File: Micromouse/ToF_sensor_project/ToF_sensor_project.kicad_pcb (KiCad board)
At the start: 2 copper layers, 5 parts, among them J2 Conn_01x06_Pin

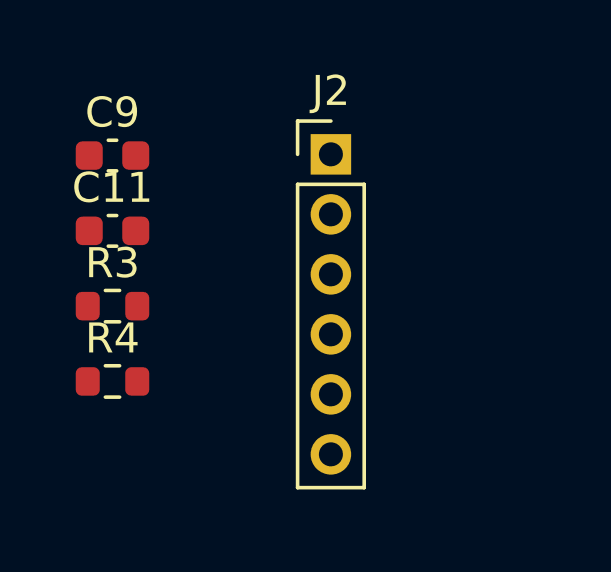
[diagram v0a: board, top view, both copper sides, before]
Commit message: Completed IR board, ToF board, changed IMU
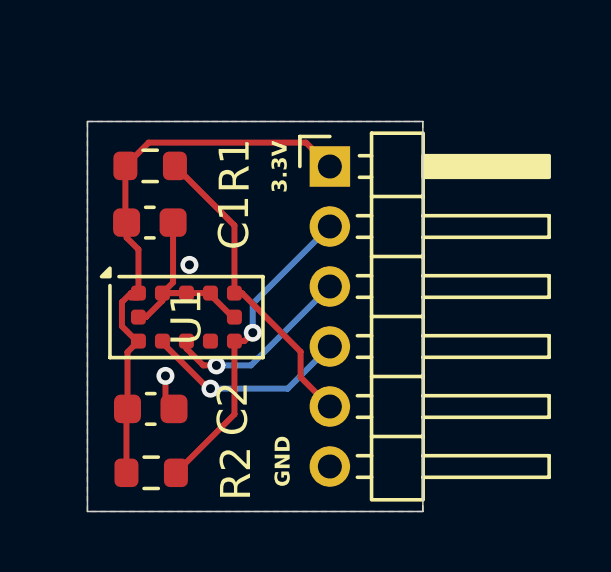
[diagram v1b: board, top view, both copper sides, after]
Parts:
- added U1: VL53L1CXV0FY1, Sensor_Distance:ST_VL53L1x, F.Cu at (149.9, 92.6)
- J1: renamed from J2; footprint Connector_PinHeader_2.00mm:PinHeader_1x06_P2.00mm_Vertical -> Connector_PinHeader_2.00mm:PinHeader_1x06_P2.00mm_Horizontal
- moved R1 7.29 mm to (148.7, 87.6)
- moved C2 6.07 mm to (148.7, 95.7), turned to 180 degrees
- moved R2 5.70 mm to (148.7, 97.8)
- moved C1 2.56 mm to (148.7, 89.5), turned to 180 degrees
- moved J1 0.41 mm to (154.7, 87.6)
- renumbered C9 to C1, C11 to C2, R4 to R1, R3 to R2
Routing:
- net +3.3V: track 0.00 -> 18.7 mm
- net Net-(J1-Pin_2): track 0.00 -> 10.5 mm, vias 0 -> 1
- net Net-(J1-Pin_5): track 0.00 -> 10.3 mm
- net GND: track 0.00 -> 8.56 mm, vias 0 -> 2
- net Net-(J1-Pin_4): track 0.00 -> 6.85 mm, vias 0 -> 1
- net Net-(J1-Pin_3): track 0.00 -> 6.60 mm, vias 0 -> 1
- added copper zone on B.Cu, net GND
- added copper zone on F.Cu, net GND
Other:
- board outline added: 11.2 x 13 mm
- board text added: "3.3V"
- board text added: "GND"
